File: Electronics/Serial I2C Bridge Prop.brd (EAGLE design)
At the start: 38.5 x 43.9 mm, 25 parts, among them IC1 24LC256SN, Q1 5MHz

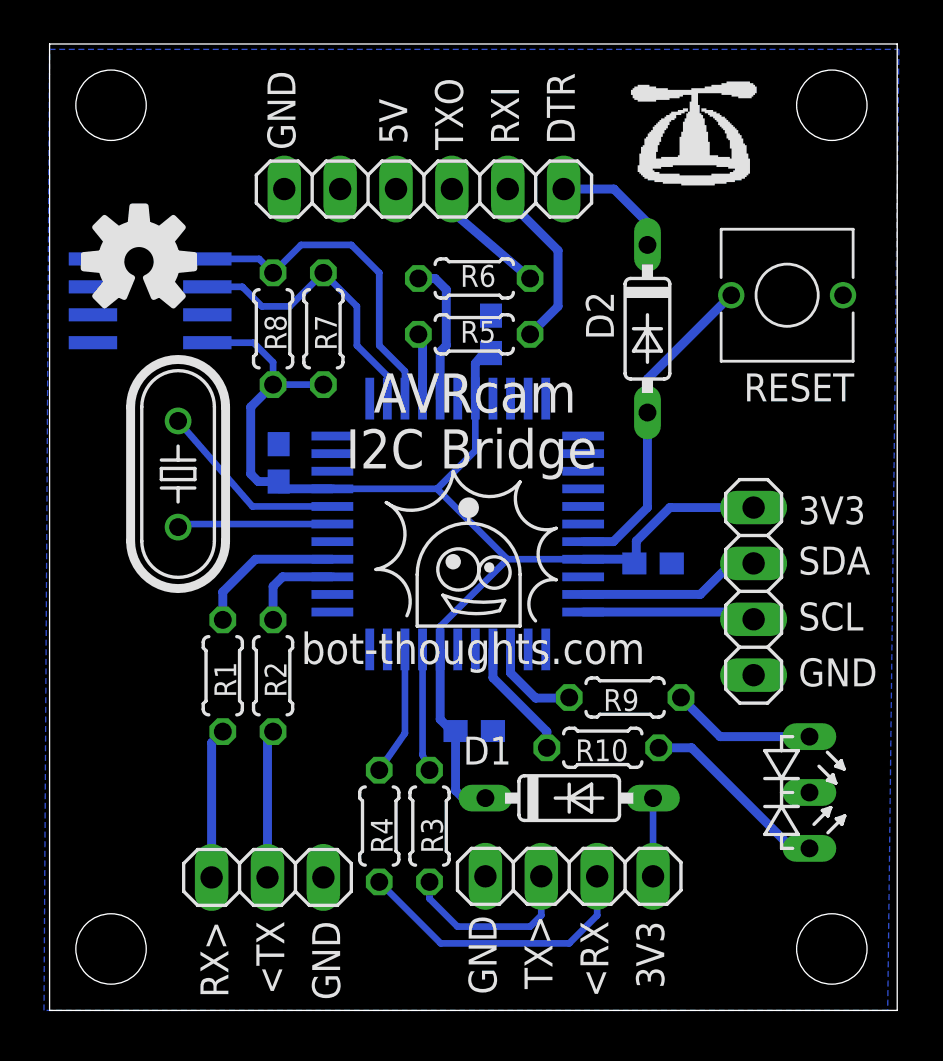
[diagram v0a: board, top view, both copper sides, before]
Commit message: Moved RC Mux to subdirectory. Minor changes to various other boards.
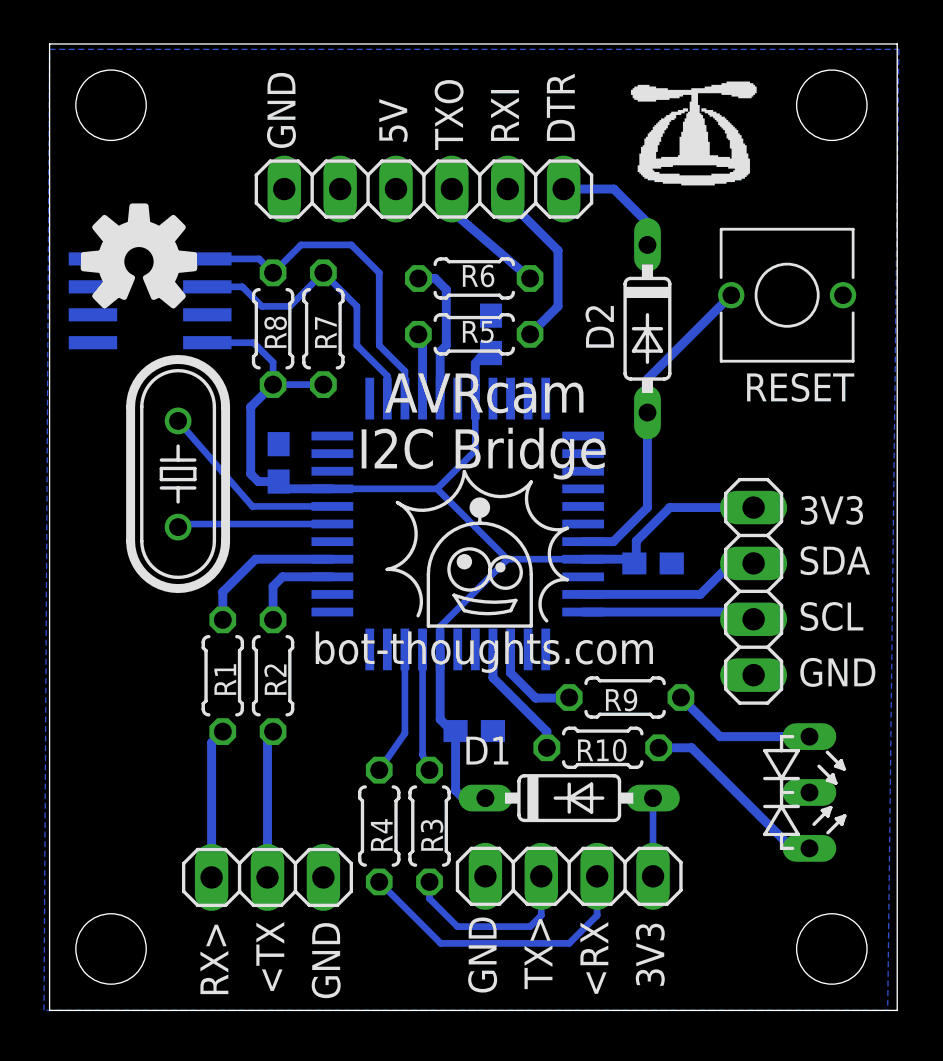
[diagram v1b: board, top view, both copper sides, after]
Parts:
- R1, R2, R3, R4, R5, R6: value 22K -> 1.8K
- R10, R9: value 330 -> 390
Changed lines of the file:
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@@
 <layer number="24" name="bOrigins" color="15" fill="1" visible="yes" active="yes"/>
 <layer number="25" name="tNames" color="7" fill="1" visible="yes" active="yes"/>
-<layer number="26" name="bNames" color="7" fill="1" visible="no" active="yes"/>
+<layer number="26" name="bNames" color="7" fill="1" visible="yes" active="yes"/>
 <layer number="27" name="tValues" color="7" fill="1" visible="yes" active="yes"/>
 <layer number="28" name="bValues" color="7" fill="1" visible="no" active="yes"/>
@@
 <layer number="50" name="dxf" color="7" fill="1" visible="no" active="no"/>
 <layer number="51" name="tDocu" color="7" fill="1" visible="yes" active="yes"/>
-<layer number="52" name="bDocu" color="7" fill="1" visible="no" active="yes"/>
+<layer number="52" name="bDocu" color="7" fill="1" visible="yes" active="yes"/>
 <layer number="53" name="tPadExt" color="7" fill="1" visible="no" active="no"/>
 <layer number="54" name="bPadExt" color="1" fill="1" visible="no" active="no"/>
@@
 <hole x="35.56" y="2.8194" drill="3.2"/>
 <hole x="2.794" y="2.8194" drill="3.2"/>
-<text x="14.732" y="27.2034" size="1.778" layer="25">AVRcam</text>
-<text x="13.462" y="24.6634" size="1.778" layer="25">I2C Bridge</text>
-<wire x1="16.710534375" y1="17.497934375" x2="21.389465625" y2="17.497934375" width="0.1524" layer="21"/>
-<wire x1="21.389465625" y1="17.497934375" x2="21.389465625" y2="19.8374" width="0.1524" layer="21"/>
-<wire x1="16.710534375" y1="17.497934375" x2="16.710534375" y2="19.8374" width="0.1524" layer="21"/>
-<wire x1="16.710534375" y1="19.8374" x2="19.05" y2="22.176865625" width="0.1524" layer="21" curve="-90"/>
-<wire x1="19.05" y1="22.176865625" x2="21.389465625" y2="19.8374" width="0.1524" layer="21" curve="-90"/>
-<wire x1="19.05" y1="22.176865625" x2="19.05" y2="22.410825" width="0.1524" layer="21"/>
-<circle x="18.58210625" y="20.071359375" radius="0.9357875" width="0.1524" layer="21"/>
-<circle x="20.219746875" y="19.930975" radius="0.715753125" width="0.1524" layer="21"/>
-<wire x1="17.880253125" y1="18.9016125" x2="20.687640625" y2="18.667653125" width="0.1524" layer="21" curve="30"/>
-<wire x1="20.687640625" y1="18.667653125" x2="20.45368125" y2="18.199759375" width="0.1524" layer="21"/>
-<wire x1="20.45368125" y1="18.199759375" x2="18.348146875" y2="18.199759375" width="0.1524" layer="21" curve="-30"/>
-<wire x1="18.348146875" y1="18.199759375" x2="17.880253125" y2="18.9016125" width="0.1524" layer="21"/>
-<wire x1="16.242640625" y1="17.965825" x2="14.838959375" y2="20.071359375" width="0.1524" layer="21" curve="120"/>
-<wire x1="14.838959375" y1="20.071359375" x2="15.306853125" y2="23.112653125" width="0.1524" layer="21" curve="140"/>
-<wire x1="15.306853125" y1="23.112653125" x2="18.348146875" y2="24.516359375" width="0.1524" layer="21" curve="120"/>
-<wire x1="18.348146875" y1="24.516359375" x2="21.389465625" y2="24.048440625" width="0.1524" layer="21" curve="120"/>
-<wire x1="21.389465625" y1="24.048440625" x2="23.02710625" y2="21.942934375" width="0.1524" layer="21" curve="140"/>
-<wire x1="23.02710625" y1="21.942934375" x2="23.02710625" y2="19.603440625" width="0.1524" layer="21" curve="140"/>
-<wire x1="23.02710625" y1="19.603440625" x2="22.09131875" y2="17.731865625" width="0.1524" layer="21" curve="140"/>
-<circle x="18.348146875" y="20.422259375" radius="0.3509" width="0" layer="21"/>
-<circle x="19.9857875" y="20.164934375" radius="0.23393125" width="0" layer="21"/>
-<circle x="19.05" y="22.87871875" radius="0.46789375" width="0" layer="21"/>
-<text x="11.43" y="15.7734" size="1.4224" layer="21">bot-thoughts.com</text>
+<text x="15.24" y="27.2034" size="1.778" layer="25">AVRcam</text>
+<text x="13.97" y="24.6634" size="1.778" layer="25">I2C Bridge</text>
+<wire x1="17.218534375" y1="17.497934375" x2="21.897465625" y2="17.497934375" width="0.1524" layer="21"/>
+<wire x1="21.897465625" y1="17.497934375" x2="21.897465625" y2="19.8374" width="0.1524" layer="21"/>
+<wire x1="17.218534375" y1="17.497934375" x2="17.218534375" y2="19.8374" width="0.1524" layer="21"/>
+<wire x1="17.218534375" y1="19.8374" x2="19.558" y2="22.176865625" width="0.1524" layer="21" curve="-90"/>
+<wire x1="19.558" y1="22.176865625" x2="21.897465625" y2="19.8374" width="0.1524" layer="21" curve="-90"/>
+<wire x1="19.558" y1="22.176865625" x2="19.558" y2="22.410825" width="0.1524" layer="21"/>
+<circle x="19.09010625" y="20.071359375" radius="0.9357875" width="0.1524" layer="21"/>
+<circle x="20.727746875" y="19.930975" radius="0.715753125" width="0.1524" layer="21"/>
+<wire x1="18.388253125" y1="18.9016125" x2="21.195640625" y2="18.667653125" width="0.1524" layer="21" curve="30"/>
+<wire x1="21.195640625" y1="18.667653125" x2="20.96168125" y2="18.199759375" width="0.1524" layer="21"/>
+<wire x1="20.96168125" y1="18.199759375" x2="18.856146875" y2="18.199759375" width="0.1524" layer="21" curve="-30"/>
+<wire x1="18.856146875" y1="18.199759375" x2="18.388253125" y2="18.9016125" width="0.1524" layer="21"/>
+<wire x1="16.750640625" y1="17.965825" x2="15.346959375" y2="20.071359375" width="0.1524" layer="21" curve="120"/>
+<wire x1="15.346959375" y1="20.071359375" x2="15.814853125" y2="23.112653125" width="0.1524" layer="21" curve="140"/>
+<wire x1="15.814853125" y1="23.112653125" x2="18.856146875" y2="24.516359375" width="0.1524" layer="21" curve="120"/>
+<wire x1="18.856146875" y1="24.516359375" x2="21.897465625" y2="24.048440625" width="0.1524" layer="21" curve="120"/>
+<wire x1="21.897465625" y1="24.048440625" x2="23.53510625" y2="21.942934375" width="0.1524" layer="21" curve="140"/>
+<wire x1="23.53510625" y1="21.942934375" x2="23.53510625" y2="19.603440625" width="0.1524" layer="21" curve="140"/>
+<wire x1="23.53510625" y1="19.603440625" x2="22.59931875" y2="17.731865625" width="0.1524" layer="21" curve="140"/>
+<circle x="18.856146875" y="20.422259375" radius="0.3509" width="0" layer="21"/>
+<circle x="20.4937875" y="20.164934375" radius="0.23393125" width="0" layer="21"/>
+<circle x="19.558" y="22.87871875" radius="0.46789375" width="0" layer="21"/>
+<text x="11.938" y="15.7734" size="1.4224" layer="21">bot-thoughts.com</text>
 <text x="16.256" y="39.3954" size="1.27" layer="21" rot="R90">5V</text>
 <text x="11.176" y="39.1414" size="1.27" layer="21" rot="R90">GND</text>
@@
 <rectangle x1="28.8671" y1="40.9575" x2="28.9433" y2="41.0337" layer="21"/>
 <rectangle x1="28.7909" y1="40.9575" x2="28.8671" y2="41.0337" layer="21"/>
-<dimension x1="0" y1="43.9574" x2="38.608" y2="43.942" x3="19.304909375" y3="46.23581875" layer="51"/>
-<dimension x1="38.532" y1="43.9574" x2="38.608" y2="0" x3="41.10999375" y3="21.983090625" layer="51"/>
 </plain>
 <attributes>
@@
 <attribute name="NAME" x="18.796" y="11.2014" size="1.27" layer="25" ratio="10"/>
 </element>
-<element name="R1" library="rcl" package="0204/5" value="22K" x="7.874" y="15.24" smashed="yes" rot="R270">
+<element name="R1" library="rcl" package="0204/5" value="1.8K" x="7.874" y="15.24" smashed="yes" rot="R270">
 <attribute name="NAME" x="8.4836" y="14.2494" size="0.9906" layer="25" ratio="10" rot="R90"/>
 </element>
-<element name="R2" library="rcl" package="0204/5" value="22K" x="10.16" y="15.24" smashed="yes" rot="R270">
+<element name="R2" library="rcl" package="0204/5" value="1.8K" x="10.16" y="15.24" smashed="yes" rot="R270">
 <attribute name="NAME" x="10.7696" y="14.2494" size="0.9906" layer="25" ratio="10" rot="R90"/>
 </element>
-<element name="R3" library="rcl" package="0204/5" value="22K" x="17.272" y="8.4074" smashed="yes" rot="R270">
+<element name="R3" library="rcl" package="0204/5" value="1.8K" x="17.272" y="8.4074" smashed="yes" rot="R270">
 <attribute name="NAME" x="17.8816" y="7.1628" size="0.9906" layer="25" ratio="10" rot="R90"/>
 </element>
-<element name="R4" library="rcl" package="0204/5" value="22K" x="14.986" y="8.4074" smashed="yes" rot="R270">
+<element name="R4" library="rcl" package="0204/5" value="1.8K" x="14.986" y="8.4074" smashed="yes" rot="R270">
 <attribute name="NAME" x="15.5956" y="7.1628" size="0.9906" layer="25" ratio="10" rot="R90"/>
 </element>
@@
 <attribute name="VALUE" x="8.763" y="35.8394" size="1.27" layer="27" rot="R90"/>
 </element>
-<element name="R6" library="rcl" package="0204/5" value="22K" x="19.304" y="33.2994" smashed="yes">
+<element name="R6" library="rcl" package="0204/5" value="1.8K" x="19.304" y="33.2994" smashed="yes">
 <attribute name="NAME" x="20.2946" y="33.909" size="0.9906" layer="25" ratio="10" rot="R180"/>
 </element>
 <element name="D2" library="diode" package="DO35-7" value="1N4148" x="27.178" y="31.0134" smashed="yes" rot="R270">
-<attribute name="NAME" x="25.654" y="30.5054" size="1.27" layer="25" ratio="10" rot="R90"/>
-</element>
-<element name="R5" library="rcl" package="0204/5" value="22K" x="19.304" y="30.7594" smashed="yes">
+<attribute name="NAME" x="25.654" y="29.9974" size="1.27" layer="25" ratio="10" rot="R90"/>
+</element>
+<element name="R5" library="rcl" package="0204/5" value="1.8K" x="19.304" y="30.7594" smashed="yes">
 <attribute name="NAME" x="20.2946" y="31.369" size="0.9906" layer="25" ratio="10" rot="R180"/>
 </element>
@@
 <attribute name="VALUE" x="28.829" y="12.4714" size="1.27" layer="27" ratio="10" rot="R270"/>
 </element>
-<element name="R9" library="rcl" package="0204/5" value="330" x="26.162" y="14.2494" smashed="yes">
+<element name="R9" library="rcl" package="0204/5" value="390" x="26.162" y="14.2494" smashed="yes">
 <attribute name="NAME" x="25.1714" y="13.6398" size="0.9906" layer="25" ratio="10"/>
 </element>
-<element name="R10" library="rcl" package="0204/5" value="330" x="25.146" y="11.9634" smashed="yes" rot="R180">
+<element name="R10" library="rcl" package="0204/5" value="390" x="25.146" y="11.9634" smashed="yes" rot="R180">
 <attribute name="NAME" x="23.9014" y="11.3538" size="0.9906" layer="25" ratio="10"/>
 </element>
